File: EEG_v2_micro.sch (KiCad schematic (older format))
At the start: 9 parts, among them U6 CC2540

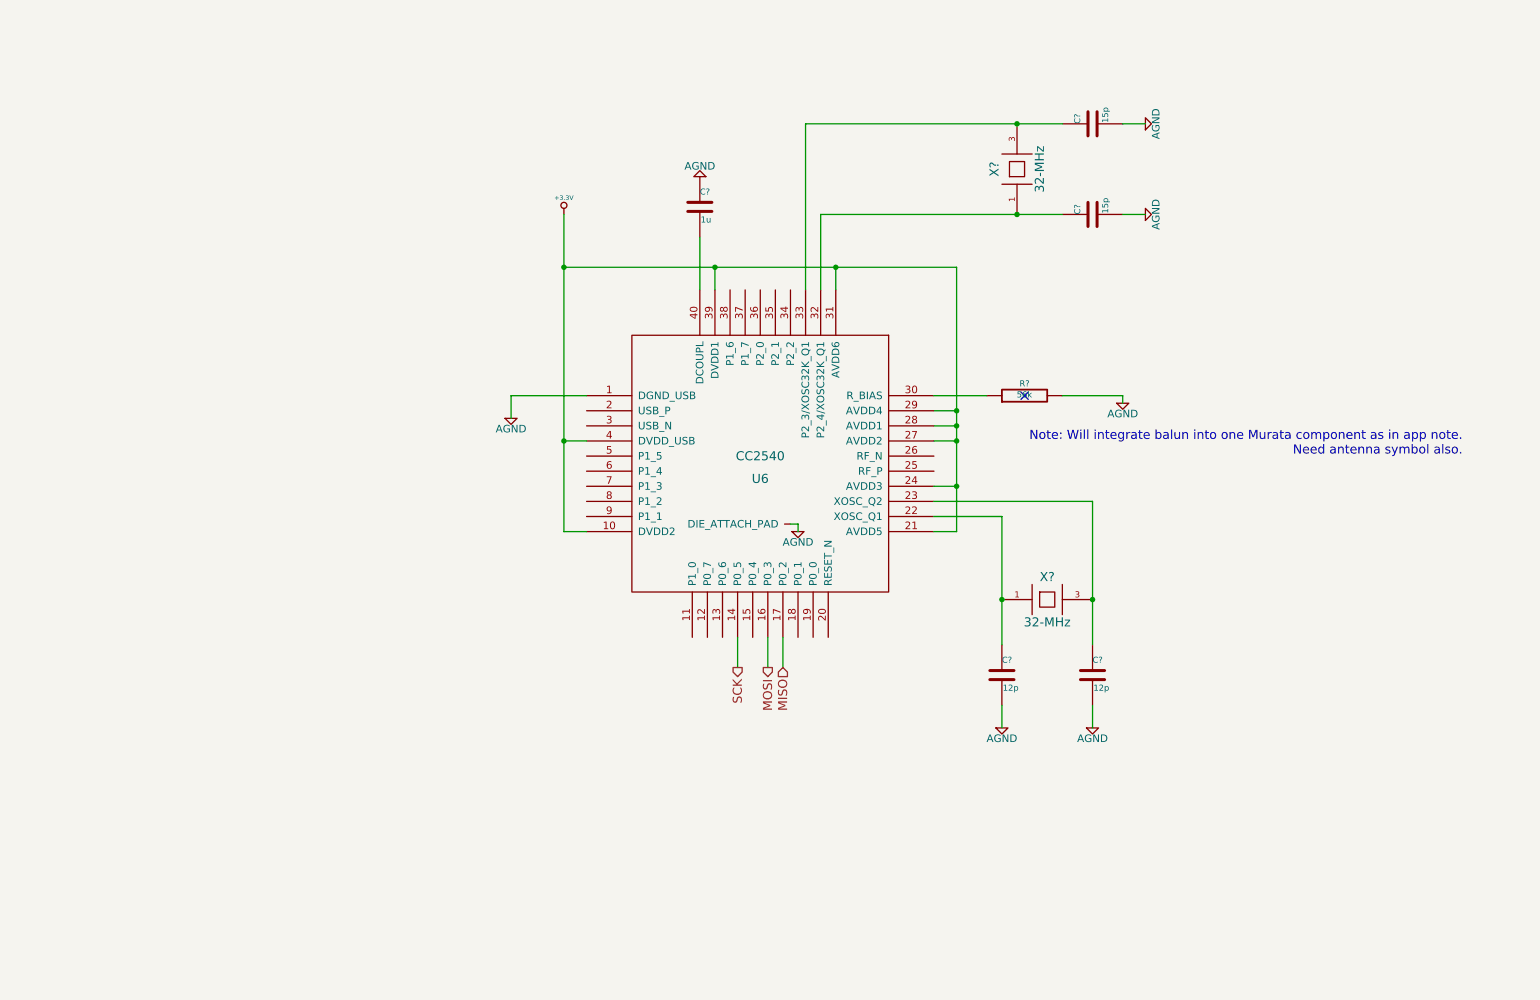
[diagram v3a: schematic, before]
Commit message: Following TI Reference design CC2540EM. Added component footprints on micro sheet.
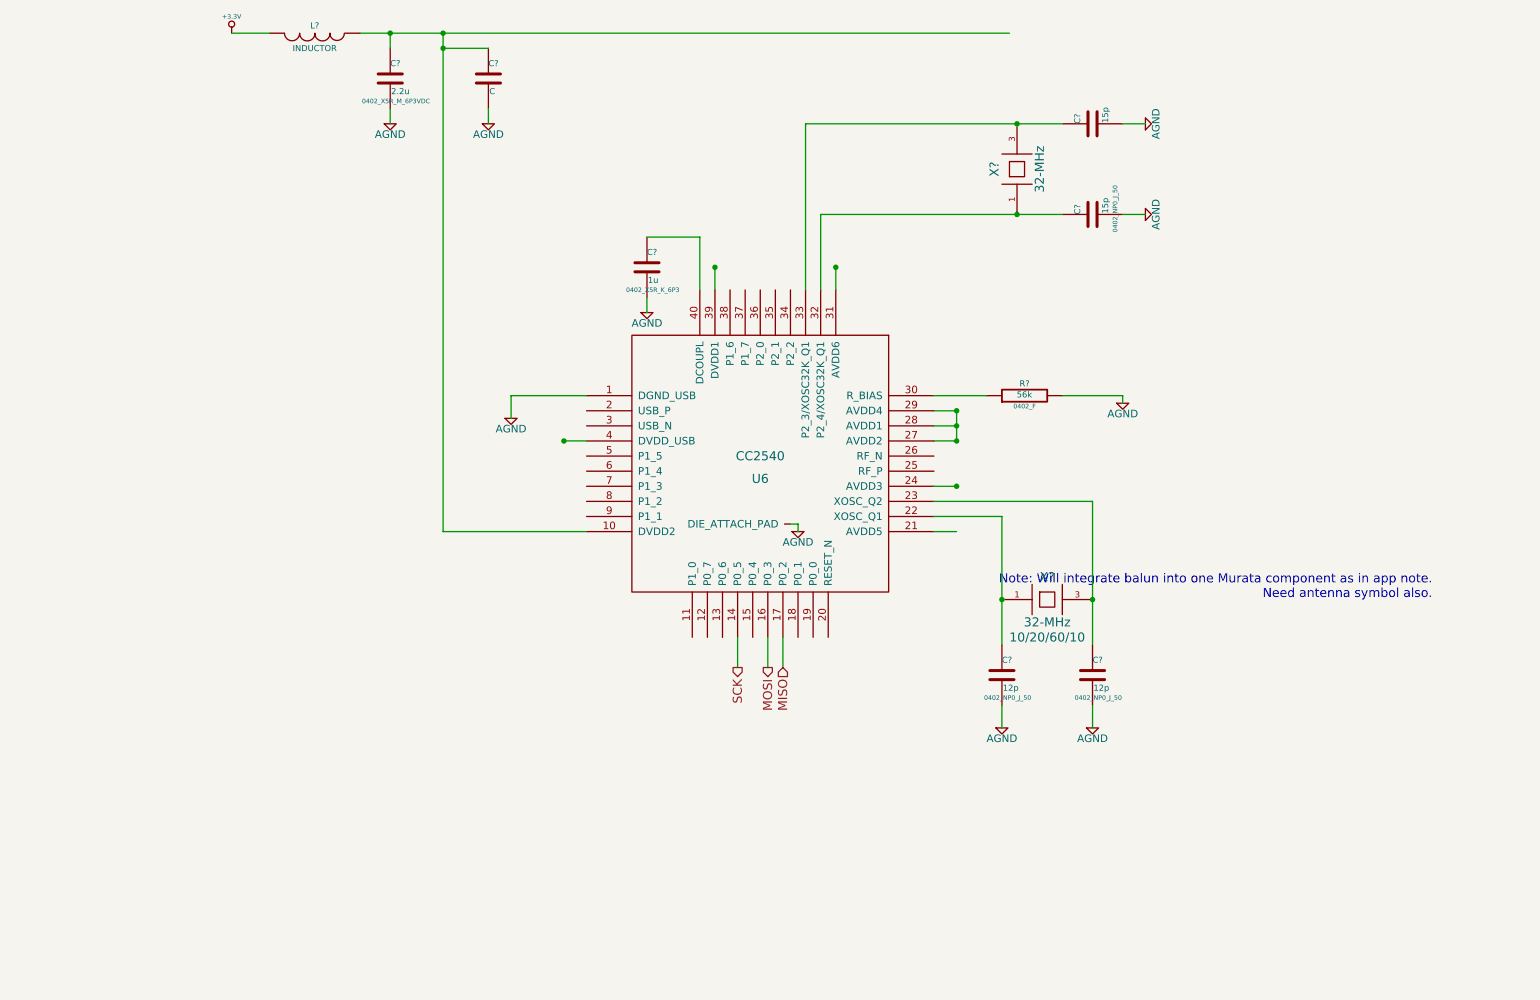
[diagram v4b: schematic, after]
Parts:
- added C?: C, ~, symbol C
- added C?: 2.2u, 0402_X5R_M_6P3VDC, symbol C
- added L?: INDUCTOR, ~, symbol INDUCTOR
- C?: footprint ~ -> 0402_X5R_K_6P3
- C? (x3): footprint ~ -> 0402_NP0_J_50
- R?: footprint ~ -> 0402_F
- X?: footprint ~ -> 10/20/60/10
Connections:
- wire segments 35 -> 42
- no-connect marks 1 -> 0
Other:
- moved on the sheet: C?
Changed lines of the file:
@@
 Sheet 4 4
 Title "Project Synapse Prototype Board"
-Date "13 jan 2015"
+Date "14 jan 2015"
 Rev "A.b"
 Comp "Senior Design 14-15"
@@
 L C C?
 U 1 1 54B4DAF5
-P 5050 2550
-F 0 "C?" H 5050 2650 40  0000 L CNN
-F 1 "1u" H 5056 2465 40  0000 L CNN
-F 2 "~" H 5088 2400 30  0000 C CNN
-F 3 "~" H 5050 2550 60  0000 C CNN
-	1    5050 2550
+P 4700 2950
+F 0 "C?" H 4700 3050 40  0000 L CNN
+F 1 "1u" H 4706 2865 40  0000 L CNN
+F 2 "0402_X5R_K_6P3" H 4738 2800 30  0000 C CNN
+F 3 "~" H 4700 2950 60  0000 C CNN
+	1    4700 2950
 	1    0    0    -1
 $EndComp
@@
 L AGND #PWR?
 U 1 1 54B4DC2F
-P 5050 2350
-F 0 "#PWR?" H 5050 2350 40  0001 C CNN
-F 1 "AGND" H 5050 2280 50  0000 C CNN
-F 2 "~" H 5050 2350 60  0000 C CNN
-F 3 "~" H 5050 2350 60  0000 C CNN
-	1    5050 2350
-	-1   0    0    1
+P 4700 3250
+F 0 "#PWR?" H 4700 3250 40  0001 C CNN
+F 1 "AGND" H 4700 3180 50  0000 C CNN
+F 2 "~" H 4700 3250 60  0000 C CNN
+F 3 "~" H 4700 3250 60  0000 C CNN
+	1    4700 3250
+	1    0    0    -1
 $EndComp
 $Comp
@@
 F 0 "R?" V 7280 3800 40  0000 C CNN
 F 1 "56k" V 7207 3801 40  0000 C CNN
-F 2 "~" V 7130 3800 30  0000 C CNN
+F 2 "0402_F" V 7130 3800 30  0000 C CNN
 F 3 "~" H 7200 3800 30  0000 C CNN
 	1    7200 3800
@@
 	6750 4700 6600 4700
 Wire Wire Line
-	6750 2950 6750 4700
+	6750 3900 6750 4100
 Wire Wire Line
 	6750 4400 6600 4400
@@
 Connection ~ 6750 4000
 Wire Wire Line
-	4150 2950 6750 2950
-Wire Wire Line
 	5950 2950 5950 3100
 Connection ~ 6750 3900
@@
 Connection ~ 5950 2950
 Wire Wire Line
-	4150 2600 4150 4700
-Wire Wire Line
 	4150 4100 4300 4100
 Connection ~ 5150 2950
 Wire Wire Line
-	4150 4700 4300 4700
+	3350 4700 4300 4700
 Connection ~ 4150 4100
-Connection ~ 4150 2950
 $Comp
 L +3.3V #PWR?
 U 1 1 54B4DF64
-P 4150 2600
-F 0 "#PWR?" H 4150 2560 30  0001 C CNN
-F 1 "+3.3V" H 4150 2710 30  0000 C CNN
-F 2 "~" H 4150 2600 60  0000 C CNN
-F 3 "~" H 4150 2600 60  0000 C CNN
-	1    4150 2600
+P 1950 1400
+F 0 "#PWR?" H 1950 1360 30  0001 C CNN
+F 1 "+3.3V" H 1950 1510 30  0000 C CNN
+F 2 "~" H 1950 1400 60  0000 C CNN
+F 3 "~" H 1950 1400 60  0000 C CNN
+	1    1950 1400
 	1    0    0    -1
 $EndComp
@@
 F 0 "X?" H 7350 5300 60  0000 C CNN
 F 1 "32-MHz" H 7350 5000 60  0000 C CNN
-F 2 "~" H 7350 5150 60  0000 C CNN
+F 2 "10/20/60/10" H 7350 4900 60  0000 C CNN
 F 3 "~" H 7350 5150 60  0000 C CNN
 	1    7350 5150
@@
 F 0 "C?" H 7050 5750 40  0000 L CNN
 F 1 "12p" H 7056 5565 40  0000 L CNN
-F 2 "~" H 7088 5500 30  0000 C CNN
+F 2 "0402_NP0_J_50" H 7088 5500 30  0000 C CNN
 F 3 "~" H 7050 5650 60  0000 C CNN
 	1    7050 5650
@@
 F 0 "C?" H 7650 5750 40  0000 L CNN
 F 1 "12p" H 7656 5565 40  0000 L CNN
-F 2 "~" H 7688 5500 30  0000 C CNN
+F 2 "0402_NP0_J_50" H 7688 5500 30  0000 C CNN
 F 3 "~" H 7650 5650 60  0000 C CNN
 	1    7650 5650
@@
 F 0 "C?" H 7650 2700 40  0000 L CNN
 F 1 "15p" H 7656 2515 40  0000 L CNN
-F 2 "~" H 7688 2450 30  0000 C CNN
+F 2 "0402_NP0_J_50" H 7688 2450 30  0000 C CNN
 F 3 "~" H 7650 2600 60  0000 C CNN
 	1    7650 2600
@@
 Text HLabel 5300 5600 3    60   Output ~ 0
 SCK
-NoConn ~ 7200 3800
 Wire Wire Line
 	5300 5400 5300 5600
@@
 Wire Wire Line
 	5600 5400 5600 5600
-Text Notes 10100 4200 2    60   ~ 0
+Text Notes 9900 5150 2    60   ~ 0
 Note: Will integrate balun into one Murata component as in app note.\n Need antenna symbol also.
+$Comp
+L C C?
+U 1 1 54B6FDC9
+P 3650 1700
+F 0 "C?" H 3650 1800 40  0000 L CNN
+F 1 "C" H 3656 1615 40  0000 L CNN
+F 2 "~" H 3688 1550 30  0000 C CNN
+F 3 "~" H 3650 1700 60  0000 C CNN
+	1    3650 1700
+	1    0    0    -1
+$EndComp
+$Comp
+L C C?
+U 1 1 54B6FDD8
+P 3000 1700
+F 0 "C?" H 3000 1800 40  0000 L CNN
+F 1 "2.2u" H 3006 1615 40  0000 L CNN
+F 2 "0402_X5R_M_6P3VDC" H 3038 1550 30  0000 C CNN
+F 3 "~" H 3000 1700 60  0000 C CNN
+	1    3000 1700
+	1    0    0    -1
+$EndComp
+Wire Wire Line
+	4700 3150 4700 3250
+Wire Wire Line
+	5050 2750 4700 2750
+$Comp
+L INDUCTOR L?
+U 1 1 54B6FE82
+P 2500 1400
+F 0 "L?" V 2450 1400 40  0000 C CNN
+F 1 "INDUCTOR" V 2600 1400 40  0000 C CNN
+F 2 "~" H 2500 1400 60  0000 C CNN
+F 3 "~" H 2500 1400 60  0000 C CNN
+	1    2500 1400
+	0    1    1    0
+$EndComp
+Wire Wire Line
+	1950 1400 2200 1400
+$Comp
+L AGND #PWR?
+U 1 1 54B6FF14
+P 3650 2000
+F 0 "#PWR?" H 3650 2000 40  0001 C CNN
+F 1 "AGND" H 3650 1930 50  0000 C CNN
+F 2 "~" H 3650 2000 60  0000 C CNN
+F 3 "~" H 3650 2000 60  0000 C CNN
+	1    3650 2000
+	1    0    0    -1
+$EndComp
+Wire Wire Line
+	3650 1900 3650 2000
+Wire Wire Line
+	2800 1400 7100 1400
+Connection ~ 3000 1400
+Wire Wire Line
+	3350 1400 3350 4700
+Connection ~ 3350 1400
+Wire Wire Line
+	3000 1400 3000 1500
+Wire Wire Line
+	3650 1500 3350 1500
+Connection ~ 3350 1500
+$Comp
+L AGND #PWR?
+U 1 1 54B7020B
+P 3000 2000
+F 0 "#PWR?" H 3000 2000 40  0001 C CNN
+F 1 "AGND" H 3000 1930 50  0000 C CNN
+F 2 "~" H 3000 2000 60  0000 C CNN
+F 3 "~" H 3000 2000 60  0000 C CNN
+	1    3000 2000
+	1    0    0    -1
+$EndComp
+Wire Wire Line
+	3000 1900 3000 2000
 $EndSCHEMATC

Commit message: Finished copy of reference design. Still need to figure out what to do with USB pins. Added Johanson balun.
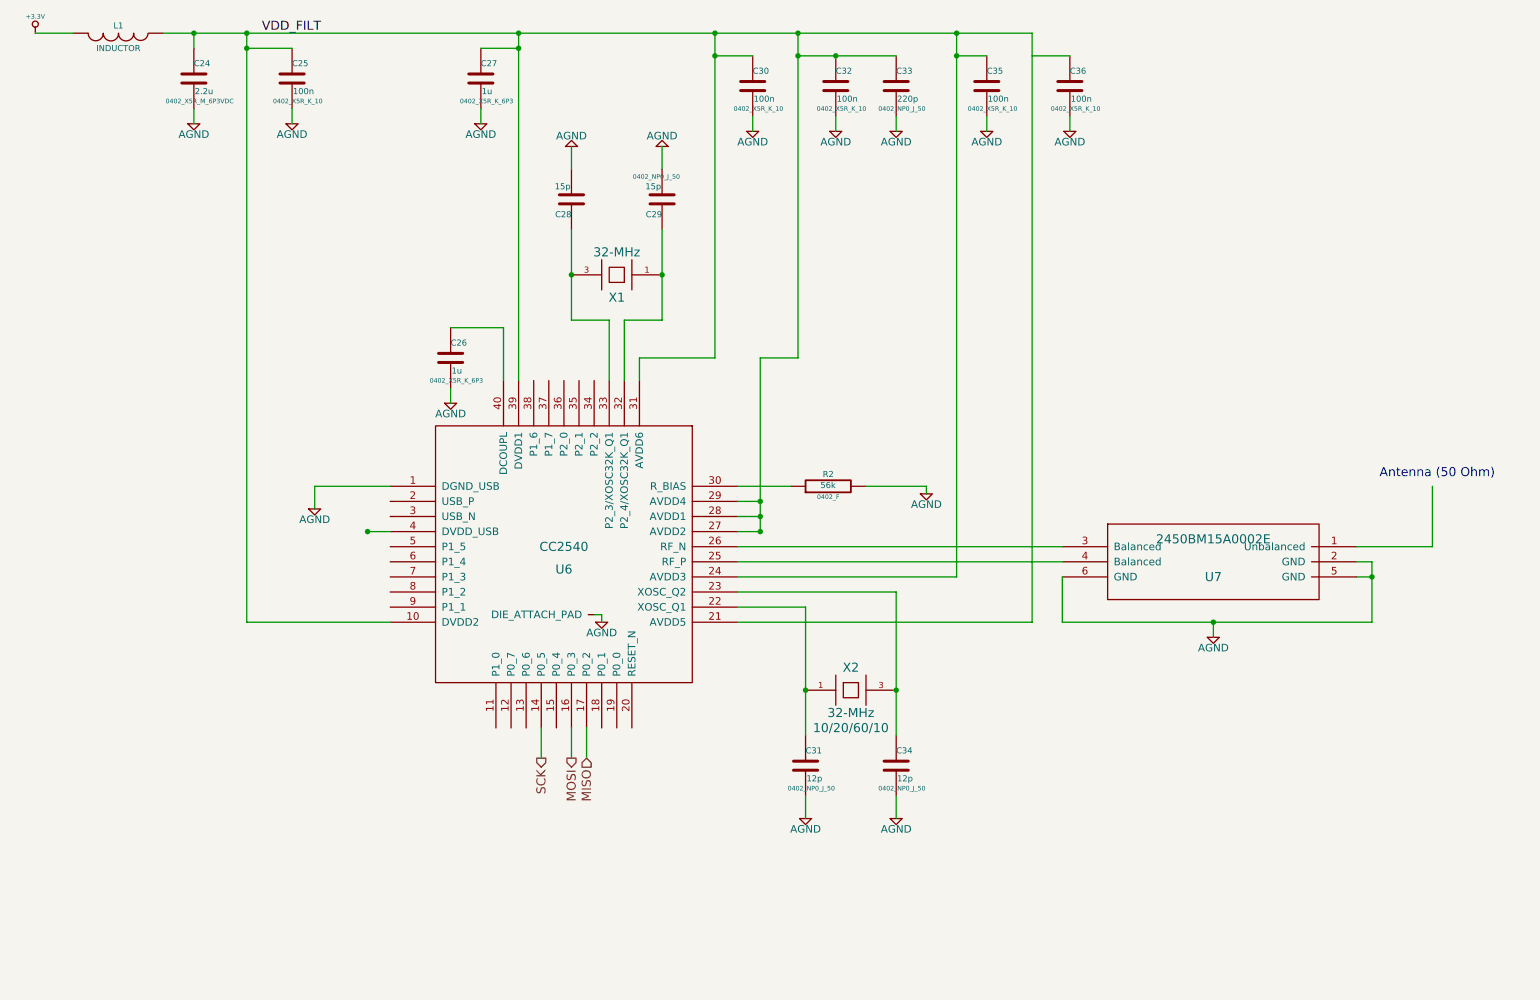
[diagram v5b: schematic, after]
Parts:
- added C27: 1u, 0402_X5R_K_6P3, symbol C
- added C30, C32, C35, C36: 100n, 0402_X5R_K_10, symbol C
- added C33: 220p, 0402_NP0_J_50, symbol C
- added U7: 2450BM15A0002E, ~, symbol 2450BM15A0002E
- C25: renamed from C?; value C -> 100n; footprint ~ -> 0402_X5R_K_10
- gave numbers to parts that had none: 10
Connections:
- net labels added: VDD_FILT
- wire segments 42 -> 71
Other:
- note added: "Antenna (50 Ohm)"
- note removed: "Note: Will integrate balun into one Murata component as in app note.\n Need antenna symbol also."
- moved on the sheet: C24, C25, C26, C28, C29, C31, C34, L1, R2, U6, X1, X2
